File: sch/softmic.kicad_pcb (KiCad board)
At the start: 2 copper layers, 101.6 x 62.2 mm, 73 parts, among them J1 USB-C, J2 Conn_01x03, J3 XLR-OUT, P1 4V1, P2 4V1, P3 VccPad, Q1 MMBFJ201, Q2 BSS64AT116, SW1 SW_Push, SW2 SW_Push, U1 MCP1812BT-033, U2 MCP2221A, U3 OPA1671, U4 OPA1671, U5 BQ21040, U6 MAX11613, U7 Oled_128_32, U8 ESP32-WROOM

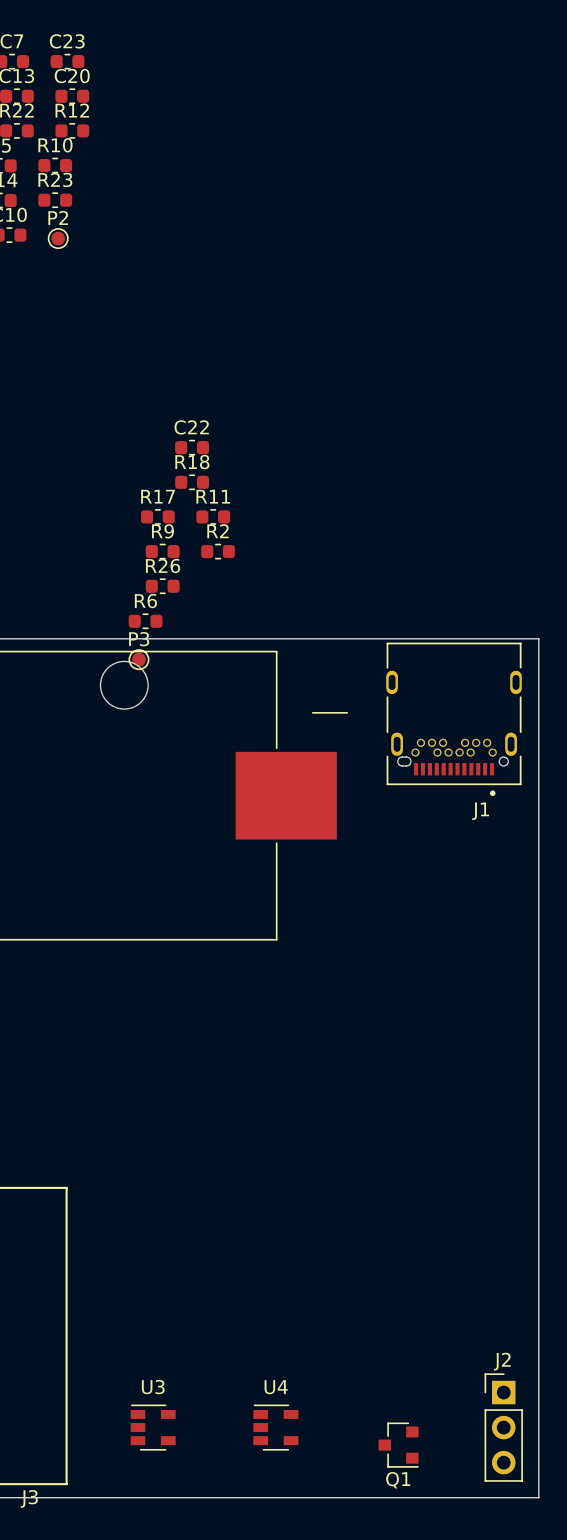
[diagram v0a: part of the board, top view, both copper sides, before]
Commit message: added line out audio jack in schematic and PCB
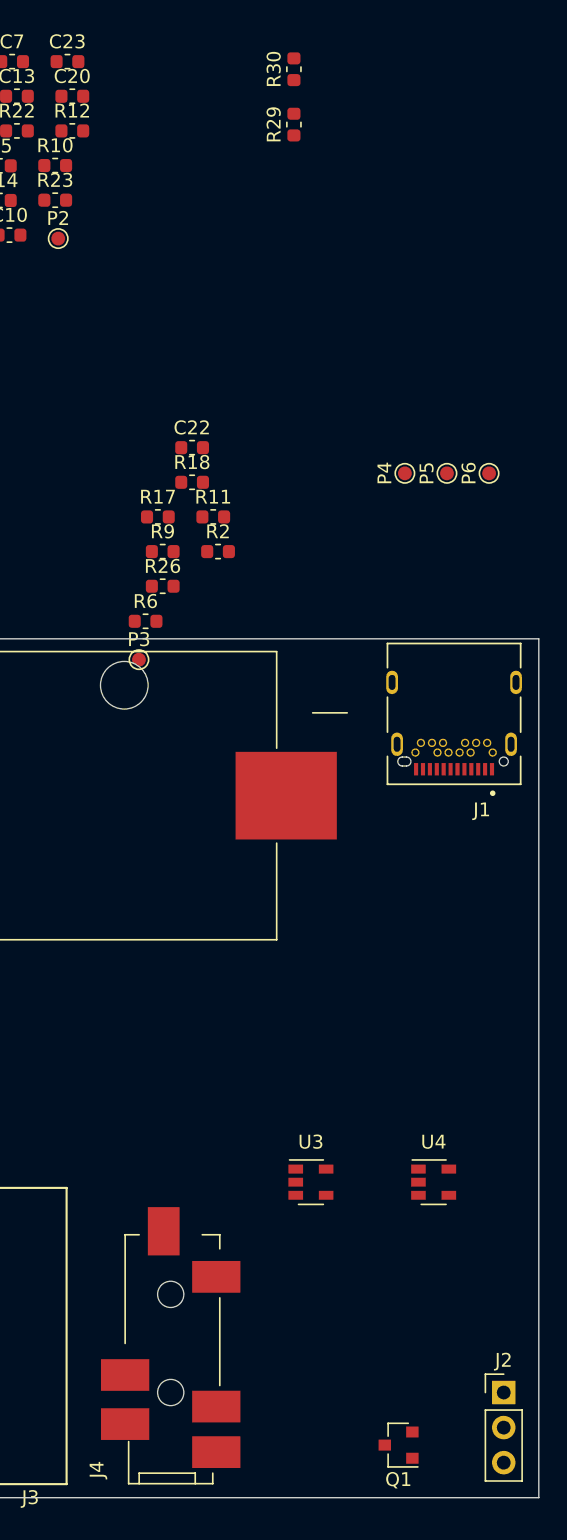
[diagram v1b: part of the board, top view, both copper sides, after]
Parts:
- added J4: AudioJack3_Ground, footprint:SJ-43514-SM, F.Cu at (163.8, 108.0)
- added P4: 4V1, TestPoint:TestPoint_Pad_D1.0mm, F.Cu at (180.8, 46.4)
- added P5: 4V1, TestPoint:TestPoint_Pad_D1.0mm, F.Cu at (183.8, 46.4)
- added P6: 4V1, TestPoint:TestPoint_Pad_D1.0mm, F.Cu at (186.9, 46.4)
- added R29: 2k, Resistor_SMD:R_0603_1608Metric, F.Cu at (172.8, 21.2)
- added R30: 2k, Resistor_SMD:R_0603_1608Metric, F.Cu at (172.8, 17.2)
- BT1: value Battery_Cell -> 1-Cell Litium Battery
- moved U3 21.1 mm to (174.0, 97.8)
- moved U4 21.1 mm to (182.9, 97.8)
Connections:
- C1 pad 2: +5V -> Net-(C1-Pad2)
- U1 pad 2: +5V -> Net-(C1-Pad2)

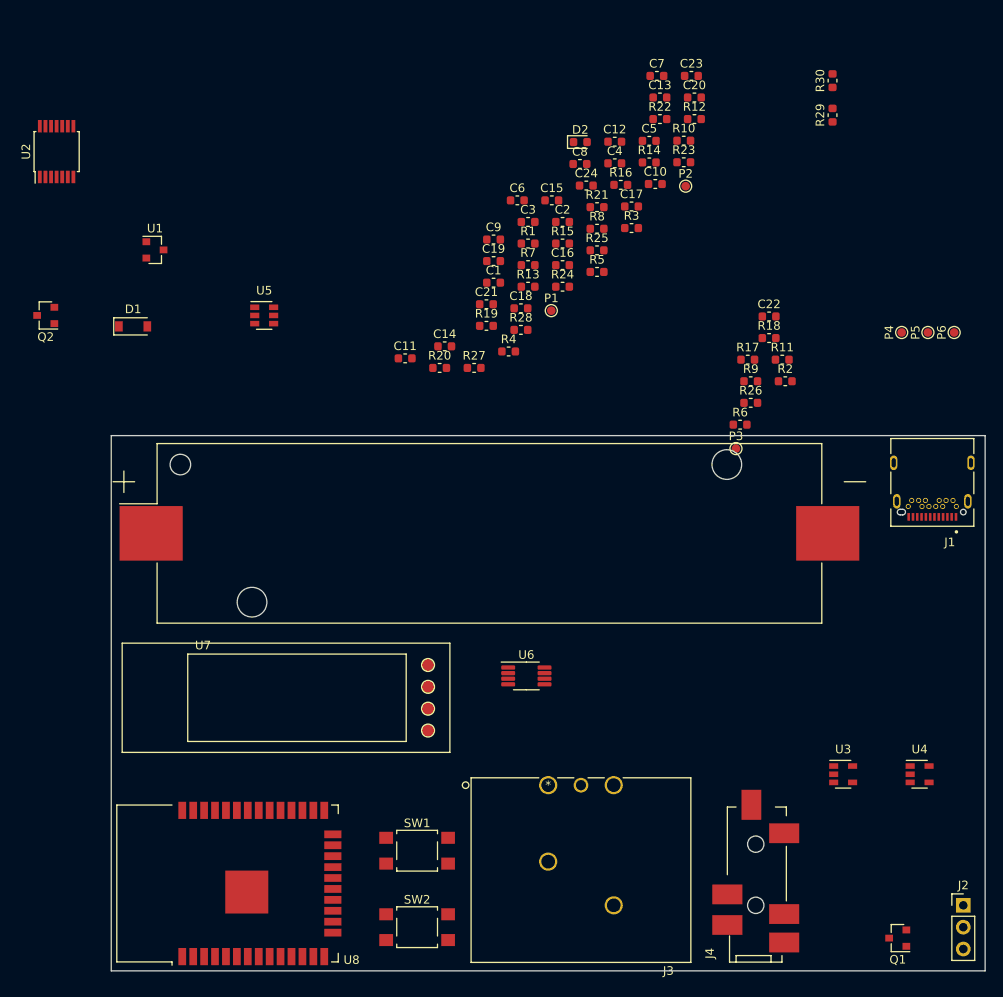
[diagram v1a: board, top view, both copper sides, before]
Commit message: changed USB to serial IC, changed some footprints, changed RST SW
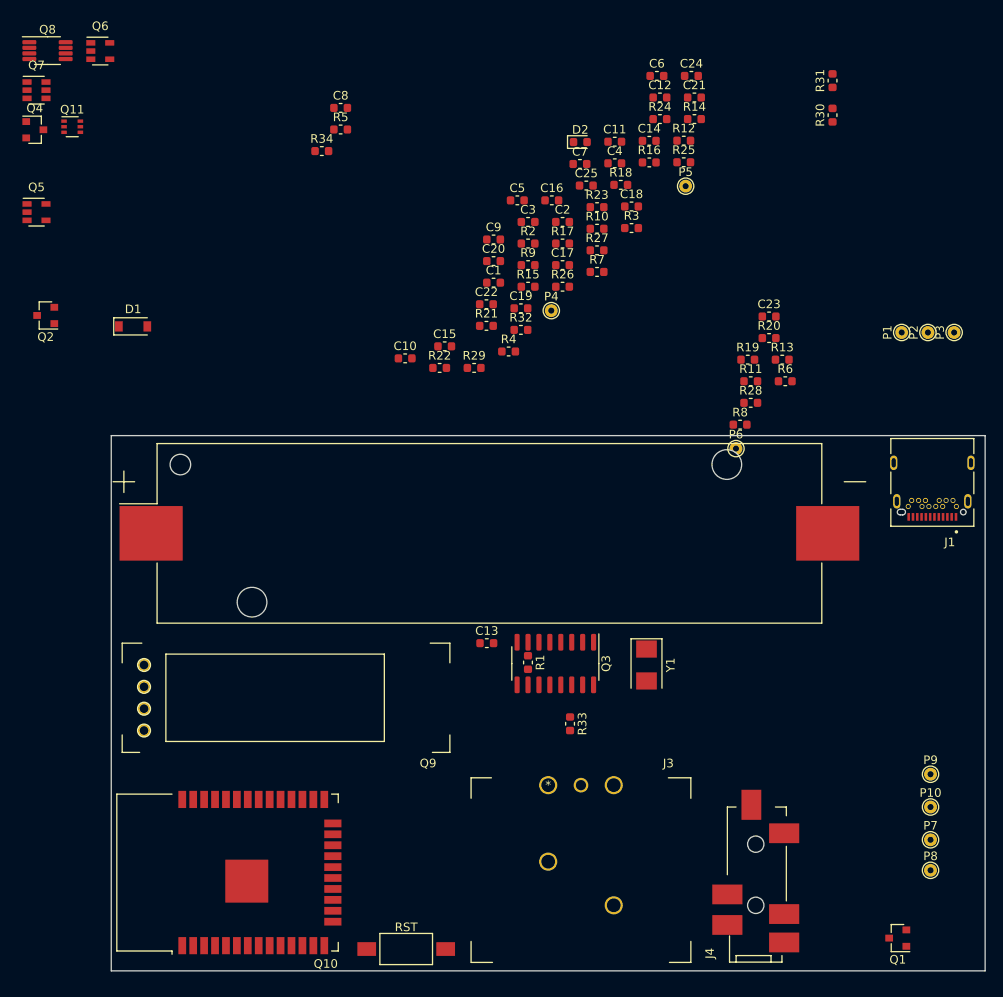
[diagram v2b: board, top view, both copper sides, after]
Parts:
- removed the C10 at (152.2, 29.2)
- removed J2: Conn_01x03, Connector_PinHeader_2.54mm:PinHeader_1x03_P2.54mm_Vertical
- removed SW2: SW_Push, Button_Switch_SMD:SW_SPST_TL3305A
- removed U1: MCP1812BT-033, Package_TO_SOT_SMD:SOT-23
- removed U2: MCP2221A, Package_SO:TSSOP-14_4.4x5mm_P0.65mm
- removed U3, U4: OPA1671, Package_TO_SOT_SMD:SOT-23-5
- removed U5: BQ21040, Package_TO_SOT_SMD:SOT-23-6
- removed U6: MAX11613, Package_SO:MSOP-8_3x3mm_P0.65mm
- removed U7: Oled_128_32, footprint:OLED-0.91-128x32
- removed U8: ESP32-WROOM, RF_Module:ESP32-WROOM-32
- added C13: 22p, Capacitor_SMD:C_0603_1608Metric, F.Cu at (132.6, 82.5)
- added C8: 22p, Capacitor_SMD:C_0603_1608Metric, F.Cu at (115.6, 20.3)
- added P10: none, TestPoint:TestPoint_THTPad_D1.5mm_Drill0.7mm, F.Cu at (184.2, 101.6)
- added P7: none, TestPoint:TestPoint_THTPad_D1.5mm_Drill0.7mm, F.Cu at (184.2, 105.4)
- added P8: none, TestPoint:TestPoint_THTPad_D1.5mm_Drill0.7mm, F.Cu at (184.2, 109.0)
- added P9: none, TestPoint:TestPoint_THTPad_D1.5mm_Drill0.7mm, F.Cu at (184.2, 97.8)
- added Q10: ESP32-WROOM, RF_Module:ESP32-WROOM-32, F.Cu at (105.4, 109.2)
- added Q11: BC847BS-TP, Package_TO_SOT_SMD:SOT-363_SC-70-6, F.Cu at (84.4, 22.5)
- added Q3: CH340G, Package_SO:SOIC-16_3.9x9.9mm_P1.27mm, F.Cu at (140.5, 84.9)
- added Q4: BSS64AT116, Package_TO_SOT_SMD:SOT-23, F.Cu at (80.0, 22.9)
- added Q5: OPA1671, Package_TO_SOT_SMD:SOT-23-5, F.Cu at (80.2, 32.4)
- added Q6: OPA1671, Package_TO_SOT_SMD:SOT-23-5, F.Cu at (87.6, 13.7)
- added Q7: BQ21040, Package_TO_SOT_SMD:SOT-23-6, F.Cu at (80.2, 18.3)
- added Q8: MAX11613, Package_SO:MSOP-8_3x3mm_P0.65mm, F.Cu at (81.5, 13.7)
- added Q9: Oled_128_32, footprint:OLED-0.91-128x32, F.Cu at (120.7, 94.0)
- added R1: 470, Resistor_SMD:R_0603_1608Metric, F.Cu at (137.3, 84.8)
- added R33: 10k, Resistor_SMD:R_0603_1608Metric, F.Cu at (142.2, 91.9)
- added R34: 10k, Resistor_SMD:R_0603_1608Metric, F.Cu at (113.4, 25.3)
- added R5: 470, Resistor_SMD:R_0603_1608Metric, F.Cu at (115.6, 22.8)
- added Y1: 12MHz, Crystal:Crystal_SMD_5032-2Pin_5.0x3.2mm, F.Cu at (151.1, 85.1)
- J4: value AudioJack3_Ground -> AudioJack 3.5mm
- P1: renamed from P4; footprint TestPoint:TestPoint_Pad_D1.0mm -> TestPoint:TestPoint_THTPad_D1.5mm_Drill0.7mm
- P2: renamed from P5; footprint TestPoint:TestPoint_Pad_D1.0mm -> TestPoint:TestPoint_THTPad_D1.5mm_Drill0.7mm
- P3: renamed from P6; footprint TestPoint:TestPoint_Pad_D1.0mm -> TestPoint:TestPoint_THTPad_D1.5mm_Drill0.7mm
- P4: renamed from P1; footprint TestPoint:TestPoint_Pad_D1.0mm -> TestPoint:TestPoint_THTPad_D1.5mm_Drill0.7mm
- P5: renamed from P2; footprint TestPoint:TestPoint_Pad_D1.0mm -> TestPoint:TestPoint_THTPad_D1.5mm_Drill0.7mm
- P6: renamed from P3; footprint TestPoint:TestPoint_Pad_D1.0mm -> TestPoint:TestPoint_THTPad_D1.5mm_Drill0.7mm
- Q1: value MMBFJ201 -> MCP1812BT-033
- Q2: value BSS64AT116 -> MMBFJ201
- SW1: value SW_Push -> RST; footprint Button_Switch_SMD:SW_SPST_TL3305A -> Button_Switch_SMD:SW_SPST_FSMSM
- moved SW1 11.5 mm to (123.2, 118.1)
- renumbered C11 to C10, C12 to C11, C13 to C12, C5 to C14, C14 to C15, C15 to C16, C16 to C17, C17 to C18, C18 to C19, C19 to C20, C20 to C21, C21 to C22, C22 to C23, C23 to C24, C24 to C25, C6 to C5, C7 to C6, C8 to C7, R8 to R10, R9 to R11, R10 to R12, R11 to R13, R12 to R14, R13 to R15, R14 to R16, R15 to R17, R16 to R18, R17 to R19, R1 to R2, R18 to R20, R19 to R21, R20 to R22, R21 to R23, R22 to R24, R23 to R25, R24 to R26, R25 to R27, R26 to R28, R27 to R29, R29 to R30, R30 to R31, R28 to R32, R2 to R6, R5 to R7, R6 to R8, R7 to R9
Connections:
- net /ESP_RESET renamed /ESP_EN
- C14 pad 2: +5V -> +3V3
- C7 pad 1: Net-(C8-Pad1) -> Net-(C7-Pad1)
- D1 pad 1: Net-(C8-Pad1) -> Net-(C7-Pad1)
- Q1 pad 1: /JFET_OUT -> +3V3
- Q1 pad 2: /MIC-IN1 -> Net-(C1-Pad2)
- Q1 pad 3: Net-(Q1-Pad3) -> GND
- Q2 pad 1: Net-(Q2-Pad1) -> /JFET_OUT
- Q2 pad 2: Net-(C8-Pad1) -> /MIC-IN1
- Q2 pad 3: +5V -> Net-(Q2-Pad3)
- R10 pad 2: Net-(Q2-Pad1) -> Net-(Q4-Pad1)
- R8 pad 2: Net-(Q1-Pad3) -> Net-(Q2-Pad3)
- R9 pad 1: Net-(C8-Pad1) -> Net-(C7-Pad1)

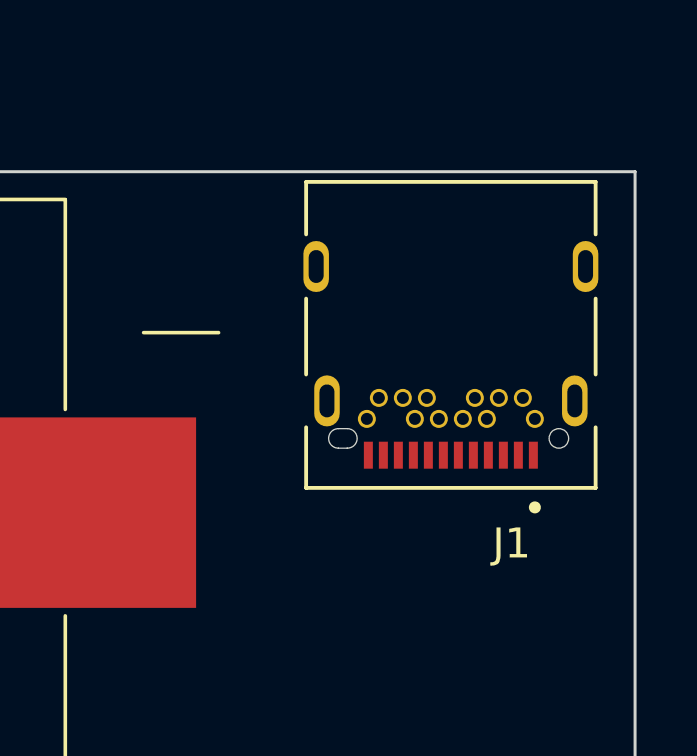
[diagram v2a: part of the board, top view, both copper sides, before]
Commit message: changed USB-C connector type
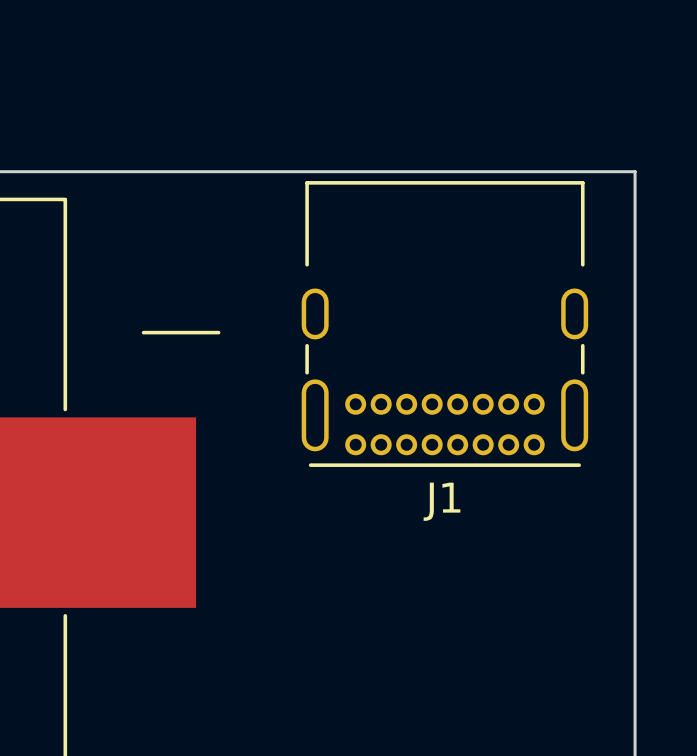
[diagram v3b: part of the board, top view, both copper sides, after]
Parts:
- J1: footprint footprint:USB-10137061-00021LF -> Connector_USB:USB_C_Receptacle_GCT_USB4085
- moved J1 0.85 mm to (187.1, 67.5)

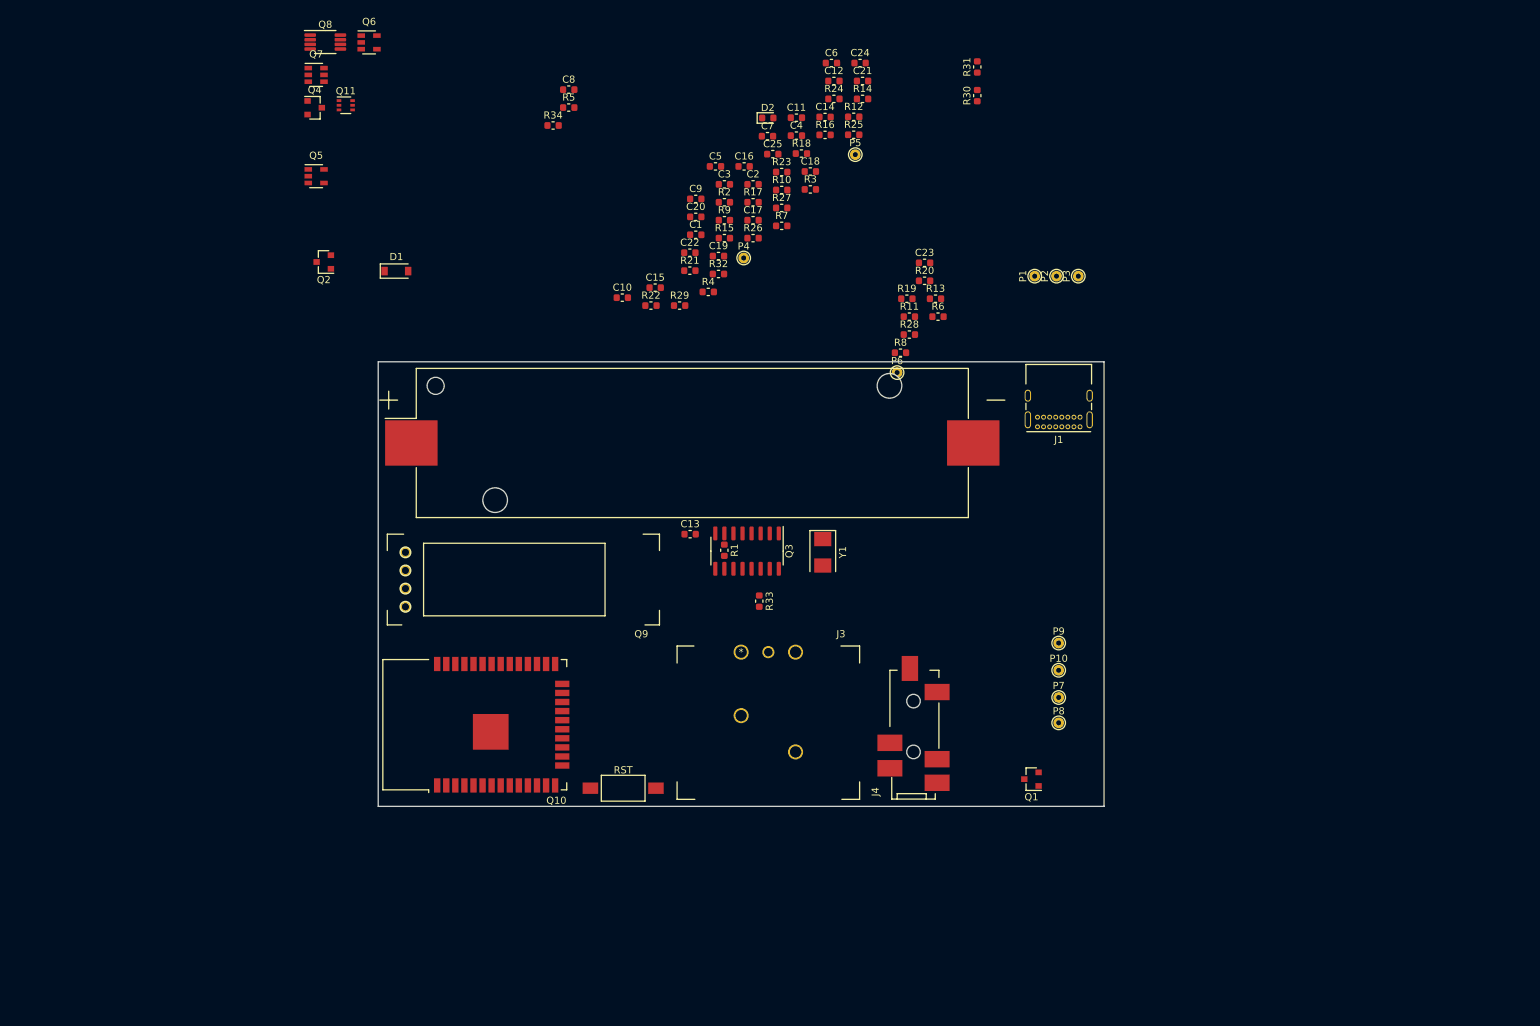
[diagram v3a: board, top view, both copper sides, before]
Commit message: changed USB-C footprint and battery holder
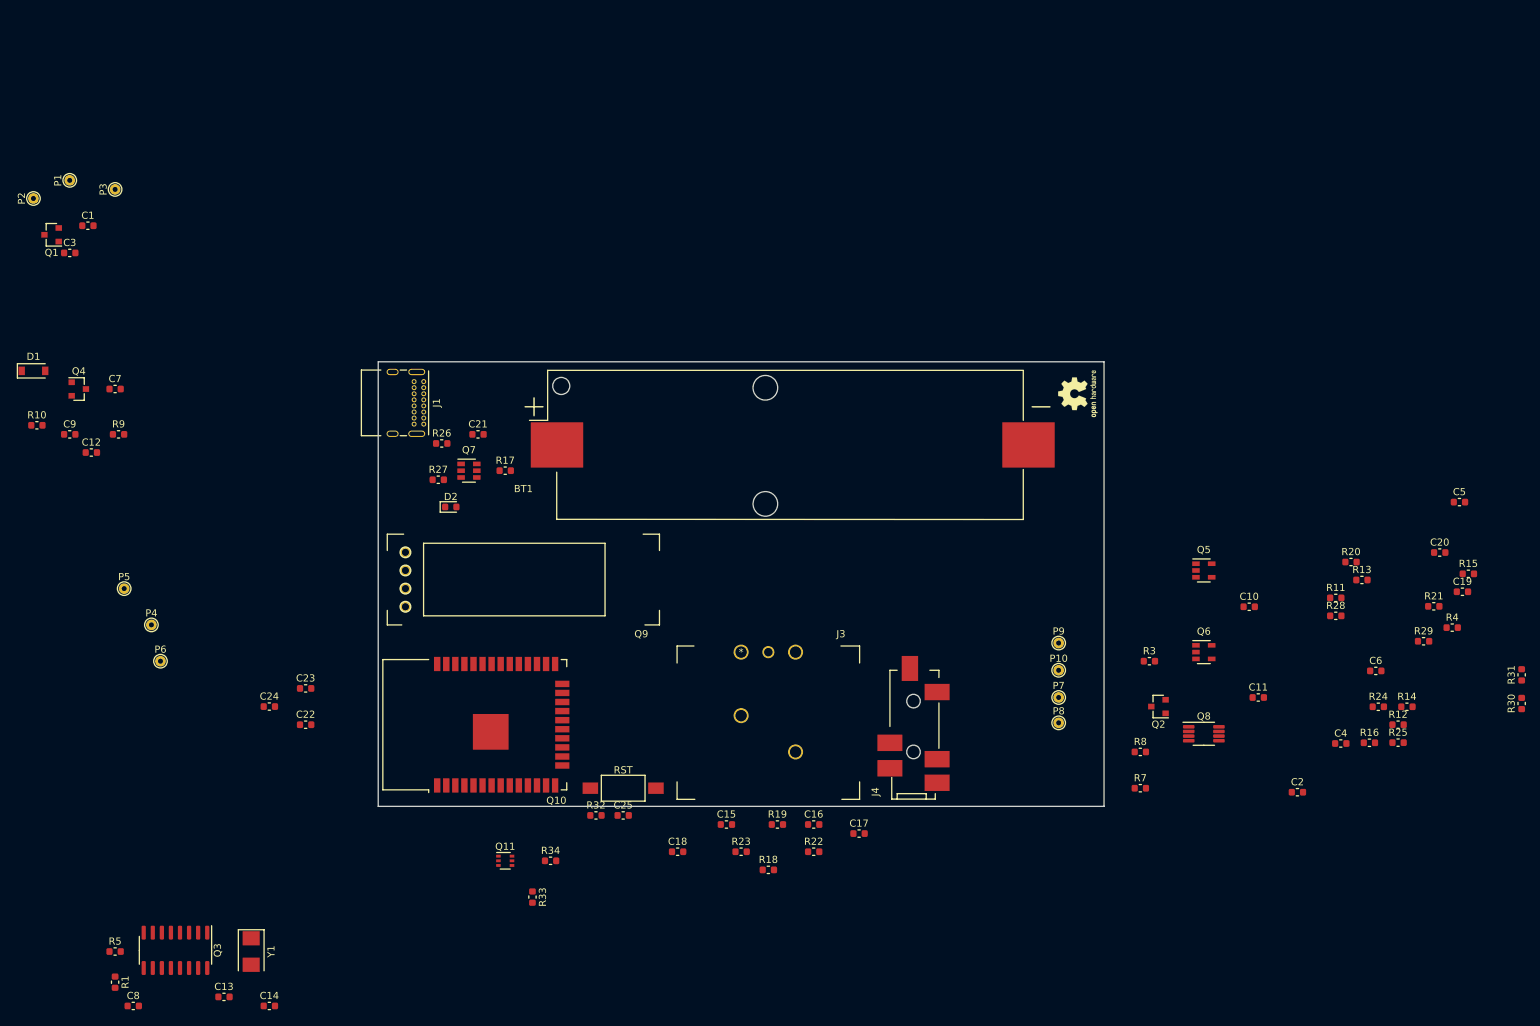
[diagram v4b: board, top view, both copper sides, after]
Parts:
- removed R2, R6: 5.1k, Resistor_SMD:R_0603_1608Metric
- added logo1: Logo_Open_Hardware_Small, Symbol:OSHW-Logo2_7.3x6mm_SilkScreen, F.Cu at (186.8, 62.9)
- BT1: footprint Battery:BatteryHolder_Keystone_1042_1x18650 -> footprint:BatteryHolder18650
- J1: value USB-C -> USB-C Connector
- moved Q1 156.9 mm to (43.2, 40.6)
- moved Q8 156.5 mm to (204.5, 110.5)
- moved C14 146.8 mm to (73.7, 148.6)
- moved Q6 144.7 mm to (204.5, 99.1)
- moved P2 143.6 mm to (40.6, 35.6)
- moved C8 142.0 mm to (54.6, 148.6)
- moved Q5 136.0 mm to (204.5, 87.6)
- moved P1 135.7 mm to (45.7, 33.0)
- moved P3 135.4 mm to (52.1, 34.3)
- moved R5 134.1 mm to (52.1, 141.0)
- moved Q2 132.4 mm to (198.1, 106.7)
- moved C24 122.3 mm to (73.7, 106.7)
- moved P5 119.0 mm to (53.3, 90.2)
- moved C12 116.2 mm to (48.7, 71.1)
- moved C20 114.3 mm to (237.5, 85.1)
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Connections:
- J1 pad B6: Net-(J1-PadB6) -> Net-(J1-PadA6)
- J1 pad B7: Net-(J1-PadB7) -> Net-(J1-PadA7)
- J1 pad S1: Net-(J1-PadS1) -> GND
- R5 pad 1: Net-(J1-PadB7) -> Net-(J1-PadA7)
